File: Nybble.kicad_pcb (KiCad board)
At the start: 2 copper layers, 250.4 x 79 mm, 106 parts, among them J1 USB_mini_micro_B, SW1 SW_PUSH, U1 ATMEGA32U4, X1 XTAL_GND

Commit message: 5 traces to go
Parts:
- moved C5 2.32 mm to (102.3, 80.9), turned to 0 degrees
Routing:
- net /Col11: track 60.7 -> 452.4 mm, vias 0 -> 1
- net /Col10: track 44.0 -> 399.7 mm
- net /Col9: track 73.7 -> 407.5 mm
- net /Col8: track 72.1 -> 388.9 mm
- net /Col7: track 64.4 -> 354.3 mm
- net Net-(R4-Pad1): track 0.00 -> 248.4 mm, vias 0 -> 2
- net Net-(R3-Pad1): track 114.6 -> 245.4 mm, vias 2 -> 4
- net /Row3: track 228.2 -> 334.2 mm, vias 0 -> 3
- net /Col0: track 65.6 -> 122.5 mm, vias 0 -> 2
- net /Row0: track 232.7 -> 275.5 mm, vias 1 -> 3
- net /Col1: track 66.5 -> 98.7 mm, vias 0 -> 2
- net /Row1: track 223.3 -> 243.9 mm, vias 2 -> 4
- net Net-(D40-Pad2): track 0.00 -> 17.8 mm
- net /Col2: track 67.3 -> 81.4 mm, vias 1 -> 2
- net Net-(R1-Pad2): track 126.7 -> 114.0 mm
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
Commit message: Finished pcb traces
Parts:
- moved R2 12.2 mm to (78.0, 77.5), turned to 225 degrees
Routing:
- net /Col6: track 44.9 -> 314.7 mm
- net /Col5: track 65.0 -> 317.8 mm
- net /Col4: track 66.3 -> 291.0 mm, vias 0 -> 1
- net /Col3: track 44.0 -> 129.7 mm, vias 0 -> 4
- net Net-(R2-Pad1): track 11.5 -> 4.72 mm
- net /Col0: track 122.5 -> 118.1 mm
- net Net-(D39-Pad2): track 17.6 -> 17.0 mm
- net /Row1: track 243.9 -> 243.8 mm, vias 4 -> 3

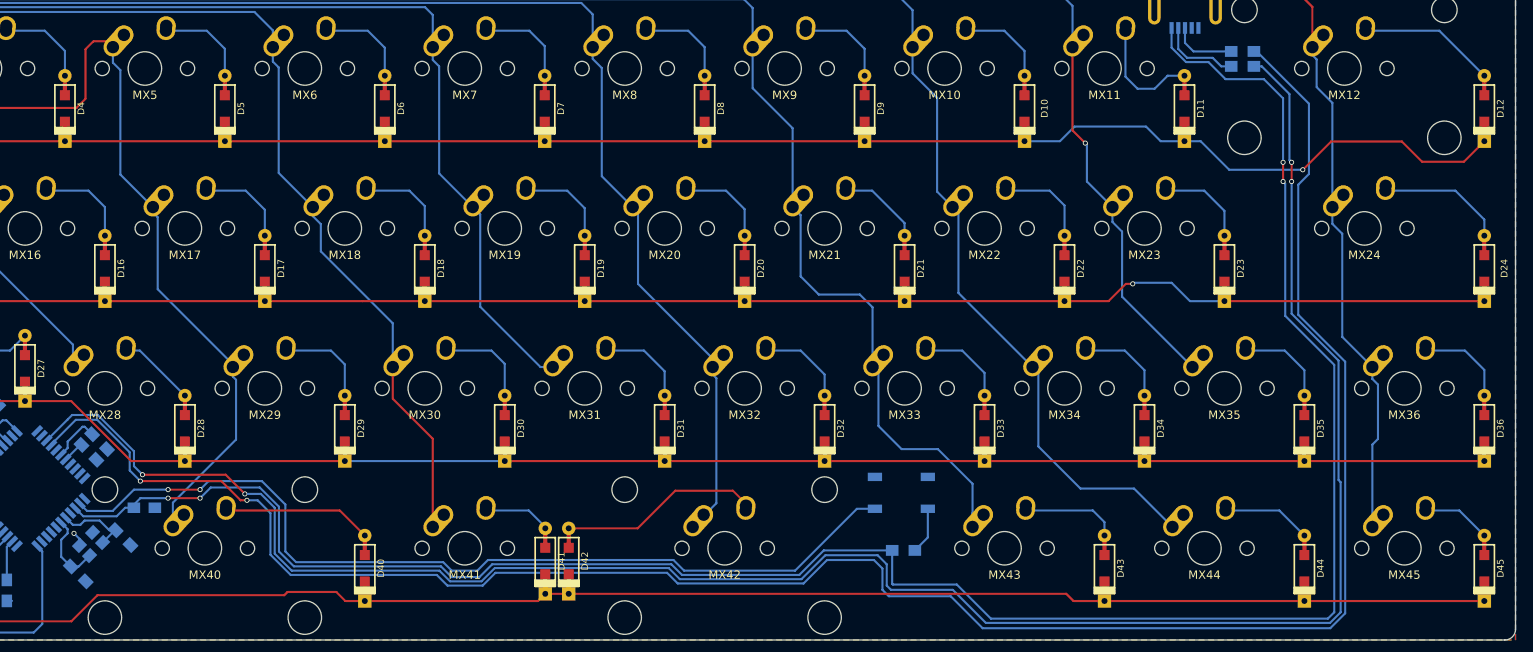
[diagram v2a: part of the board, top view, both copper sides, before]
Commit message: Fixed a few traces that were breaking the ground plane
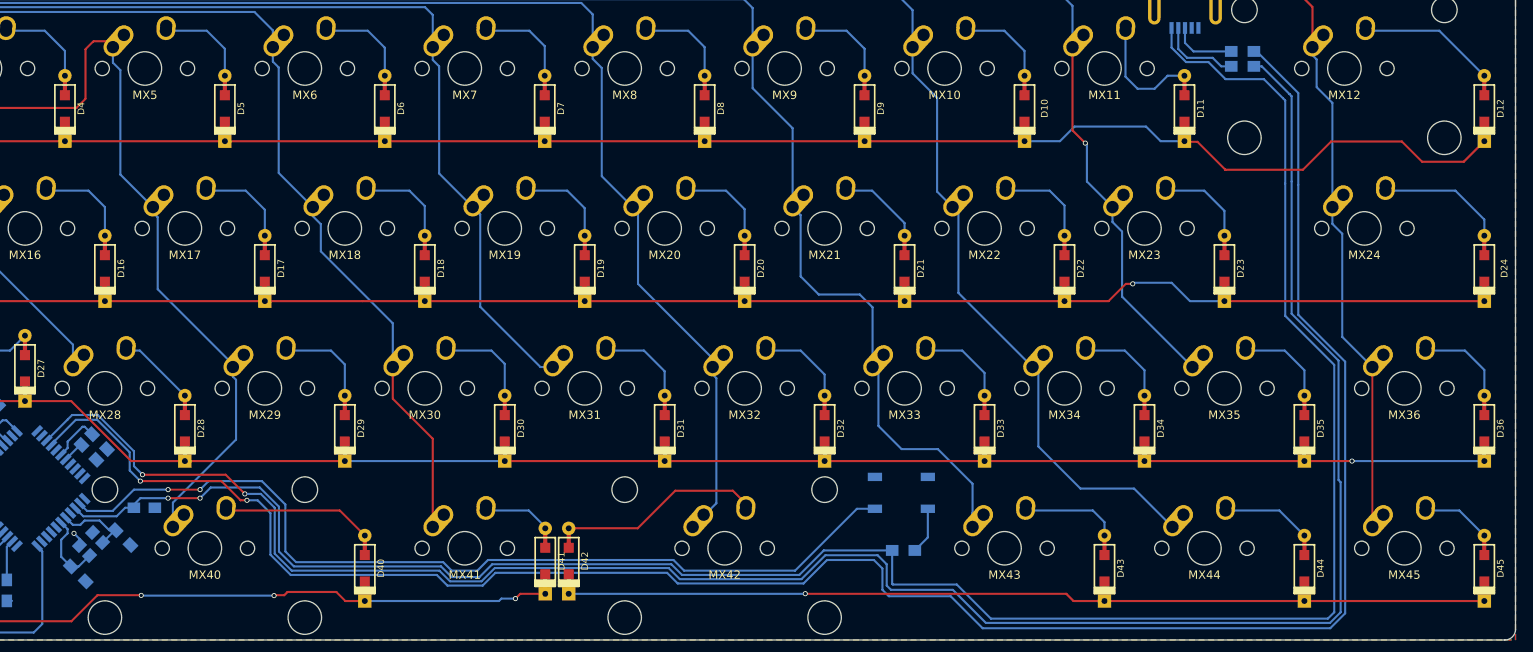
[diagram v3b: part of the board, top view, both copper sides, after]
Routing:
- net /Row3: track 334.2 -> 331.7 mm, vias 3 -> 7
- net Net-(R4-Pad1): track 248.4 -> 247.3 mm
- net /Col11: track 452.4 -> 451.9 mm
- net /Row0: vias 3 -> 2
- net Net-(R3-Pad1): vias 4 -> 2
- net /Row2: vias 2 -> 3
- net VCC: vias 4 -> 2
